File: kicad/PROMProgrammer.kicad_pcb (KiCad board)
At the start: 2 copper layers, 174.5 x 93 mm, 90 parts, among them J1 Control / Program Select Swit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, J2 USB_C_Receptacle_PowerOnly_6P, J3 Conn_01x02, J4 USB_A, J5 Barrel_Jack, Q2 BC108, Q3 BC108, Q4 BD139, Q5 BC108, Q6 BC108, SW1 SW_SPDT, SW11 SW_Push_SPDT, SW12 SW_Push_SPDT, SW13 SW_Push_SPDT, SW14 SW_Push_SPDT, SW15 SW_Push_SPDT, SW16 SW_Push_SPDT, SW17 SW_Push_SPDT, SW18 SW_Push_SPDT, SW2 SW_SPDT, SW3 SW_SPDT, SW4 SW_SPDT, SW5 SW_SPDT, SW6 SW_SPDT, SW8 SW_SPDT, U1 74S188, U2 MC34063AP, U6 4043, U7 4017, U8 HEF4093B, U9 TL431LP

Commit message: Tweak docs
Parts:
- added G003: LOGO, AAA_Project:qr_code, B.Cu at (70.4, 104.6)
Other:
- board text added: "Documentation -->"

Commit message: Starting docs
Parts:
- D10: footprint Diode_THT:D_DO-41_SOD81_P12.70mm_Horizontal -> Diode_THT:D_DO-41_SOD81_P10.16mm_Horizontal
- D14: footprint Diode_THT:D_DO-41_SOD81_P12.70mm_Horizontal -> Diode_THT:D_DO-35_SOD27_P7.62mm_Horizontal
- U1: footprint AAA_Project:DIP-16_W7.62mm_wide_TPH -> Package_DIP:DIP-16_W7.62mm
- U9: footprint Package_TO_SOT_THT:TO-92 -> Package_TO_SOT_THT:TO-92_Inline
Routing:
- net Net-(D14-A): track 33.0 -> 35.1 mm
- net PULSE: track 210.2 -> 211.5 mm
- net Net-(D10-A): track 18.6 -> 19.6 mm

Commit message: Version update
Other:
- board text added: "CS-014"
- board text added: "Version 1.4"
- board text removed: "Version 1.2"
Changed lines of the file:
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@@
 	(title_block
 		(title "PROM Programmer")
-		(date "2025-03-27")
+		(date "2025-04-06")
 		(rev "1.4")
 	)
@@
 		)
 	)
-	(gr_text "Version 1.2"
+	(gr_text "Version 1.4"
 		(at 68.956386 146.978028 0)
 		(layer "F.SilkS")
@@
 		)
 	)
+	(gr_text "CS-014"
+		(at 216.537498 144.623331 0)
+		(layer "B.SilkS")
+		(effects
+			(font
+				(size 1 1)
+				(thickness 0.1)
+			)
+			(justify left bottom mirror)
+		)
+	)

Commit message: Update docs
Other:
- board text added: "OUT IN NC"
- board text added: "Version 1.5"
- board text removed: "Version 1.4"
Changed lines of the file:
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@@
 	(title_block
 		(title "PROM Programmer")
-		(date "2025-04-06")
-		(rev "1.4")
+		(date "2025-04-14")
+		(rev "1.5")
 	)
 	(layers
@@
 		)
 		(property "Value" "10nf"
-			(at 7.907839 2.872547 0)
+			(at 2.254259 -3.410485 0)
 			(layer "F.SilkS")
 			(effects
@@
 		)
 	)
+	(gr_text "OUT IN NC"
+		(at 128.921769 63.828529 0)
+		(layer "F.SilkS")
+		(effects
+			(font
+				(size 1 1)
+				(thickness 0.25)
+				(bold yes)
+			)
+			(justify left bottom)
+		)
+	)
 	(gr_text "1"
 		(at 106.750314 95.513949 0)
@@
 	)
 	(gr_text "On"
-		(at 126.589201 61.29757 0)
+		(at 137.880796 61.224674 0)
 		(layer "F.SilkS")
 		(effects
@@
 		)
 	)
-	(gr_text "Version 1.4"
+	(gr_text "Version 1.5"
 		(at 68.956386 146.978028 0)
 		(layer "F.SilkS")
@@
 	)
 	(gr_text "Off"
-		(at 137.811318 61.407161 0)
+		(at 126.693046 61.44534 0)
 		(layer "F.SilkS")
 		(effects
@@
 	(segment
 		(start 146.466151 105.33421)
-		(end 146.466151 119.091211)
+		(end 146.466151 125.33484)
 		(width 0.5)
 		(layer "F.Cu")
@@
 		(layer "F.Cu")
 		(net 44)
-	)
-	(segment
-		(start 146.466151 119.091211)
-		(end 146.466151 125.33484)
-		(width 0.5)
-		(layer "F.Cu")
-		(net 44)

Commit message: Tidy up & docs
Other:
- board text added: "<-- Program Read -->"
- board text added: "Press To"
- board text added: "Program"
- board text removed: "<-- Program Control -->"
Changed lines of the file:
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@@
 		(layer "Edge.Cuts")
+	)
+	(gr_text "Program"
+		(at 178.790086 85.998869 0)
+		(layer "F.SilkS")
+		(effects
+			(font
+				(size 1.5 1.5)
+				(thickness 0.3)
+				(bold yes)
+			)
+			(justify left bottom)
+		)
 	)
 	(gr_text "1\n\n2\n\n3"
@@
 		)
 	)
-	(gr_text "<-- Program\n\n\n\n    Control -->"
-		(at 208.630704 82.085949 0)
+	(gr_text "<-- Program\n\n\n\n    Read -->"
+		(at 211.071613 82.133825 0)
 		(layer "F.SilkS")
 		(effects
@@
 				(bold yes)
 			)
+			(justify left bottom)
+		)
+	)
+	(gr_text "Press To"
+		(at 178.839736 74.231872 0)
+		(layer "F.SilkS")
+		(effects
+			(font
+				(size 1.5 1.5)
+				(thickness 0.3)
+				(bold yes)
+			)

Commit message: Minor layout changes
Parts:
- added TP7: GND, TestPoint:TestPoint_THTPad_2.0x2.0mm_Drill1.0mm, F.Cu at (117.4, 137.9)
- U1: footprint Package_DIP:DIP-16_W7.62mm -> Socket:DIP_Socket-16_W4.3_W5.08_W7.62_W10.16_W10.9_3M_216-3340-00-0602J
- moved C12 8.92 mm to (138.4, 116.5)
- moved C5 8.53 mm to (110.2, 62.2)
- moved U8 7.80 mm to (128.7, 121.6)
- moved TP1 5.56 mm to (138.2, 108.9)
- moved SW8 5.43 mm to (141.3, 60.7)
- moved TP2 3.28 mm to (113.4, 132.7)
- moved J4 3.20 mm to (159.2, 70.7)
- moved J5 3.20 mm to (173.7, 71.1)
- moved C4 2.47 mm to (142.2, 68.6), turned to -90 degrees
- moved RV1 2.26 mm to (159.2, 102.3)
- moved U7 1.24 mm to (145.2, 114.0)
- moved TP6 1.21 mm to (136.9, 96.1)
- moved R12 0.90 mm to (159.2, 106.2)
- moved TP3 0.73 mm to (109.6, 137.9)
- moved U6 0.72 mm to (161.7, 114.0)
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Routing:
- net +5V: track 308.7 -> 327.0 mm
- net GND: track 762.4 -> 770.6 mm
- net VCC: track 107.5 -> 100.4 mm
- net Net-(J3-Pin_1): track 97.6 -> 91.1 mm
- net Net-(C11-Pad2): track 58.6 -> 64.1 mm
- net Net-(U7-CKEN): track 25.7 -> 30.4 mm
- net Net-(U6-S2): track 47.5 -> 51.9 mm
- net Net-(C12-Pad2): track 27.6 -> 30.5 mm
- net Net-(R12-Pad1): track 5.25 -> 3.91 mm
- net START: track 31.2 -> 29.9 mm
- net Net-(U7-CLK): track 46.2 -> 47.4 mm
- net Net-(U6-S4): track 24.6 -> 23.6 mm
- net Net-(SW6-A): track 58.2 -> 57.4 mm
- net Net-(U6-Q3): track 37.1 -> 36.4 mm
- net Net-(U6-Q2): track 57.3 -> 56.6 mm
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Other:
- board text added: "!!1W HOT!!"
- board text added: "(Optional)"
- board text added: "+5V 0V"
- board text added: "053edf5b-b108-401d-a210-3ba84cfa1f3a"
- board text added: "Default Approx 4.5K"
- board text added: "Push To"
- board text added: "Version 2.0 - Layout Improvements"
- board text removed: "+5V"
- board text removed: "1W HOT!"
- board text removed: "7754d957-f0da-47ec-9f61-362ba0418017"
- board text removed: "Press To"
- board text removed: "Version 1.5"

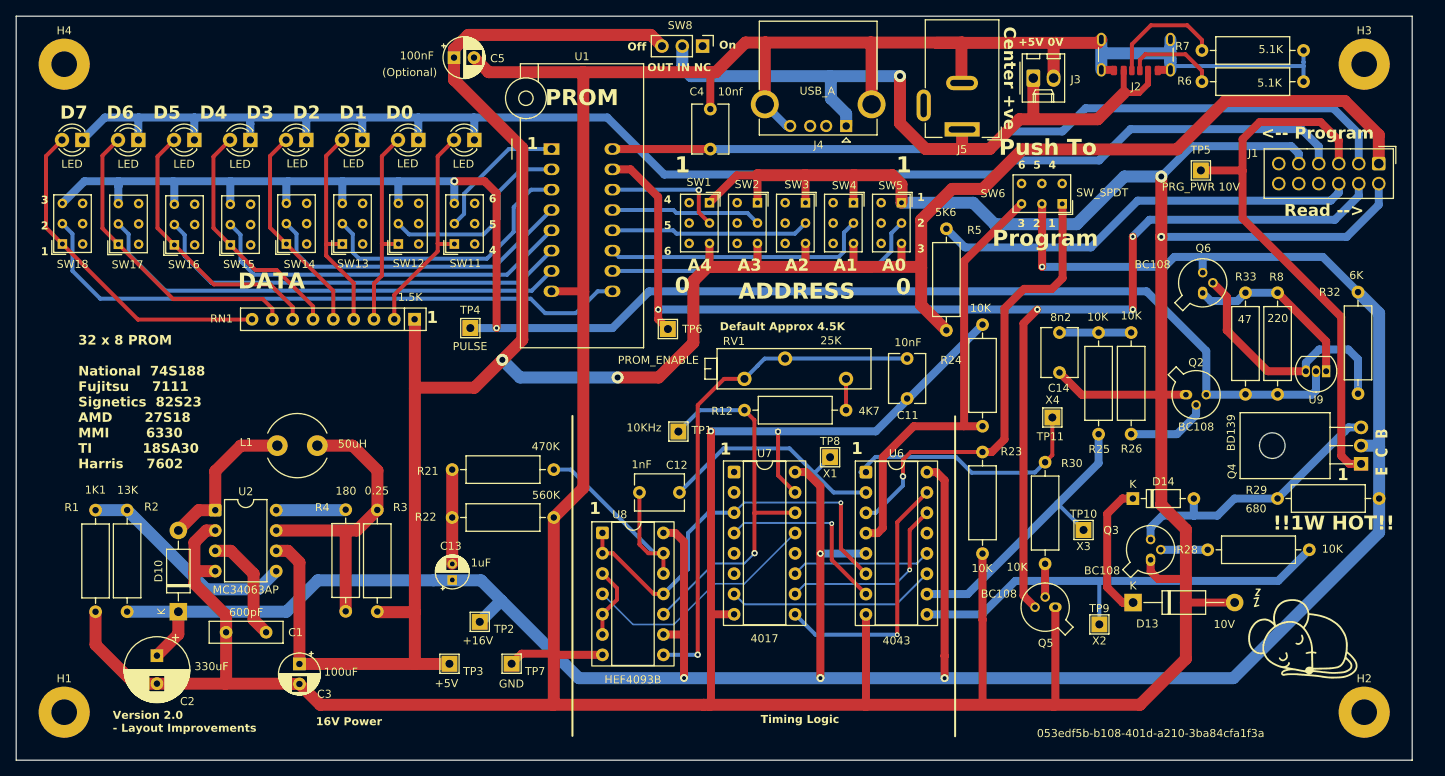
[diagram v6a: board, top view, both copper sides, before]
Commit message: Tweak layout, add part silkscreen values
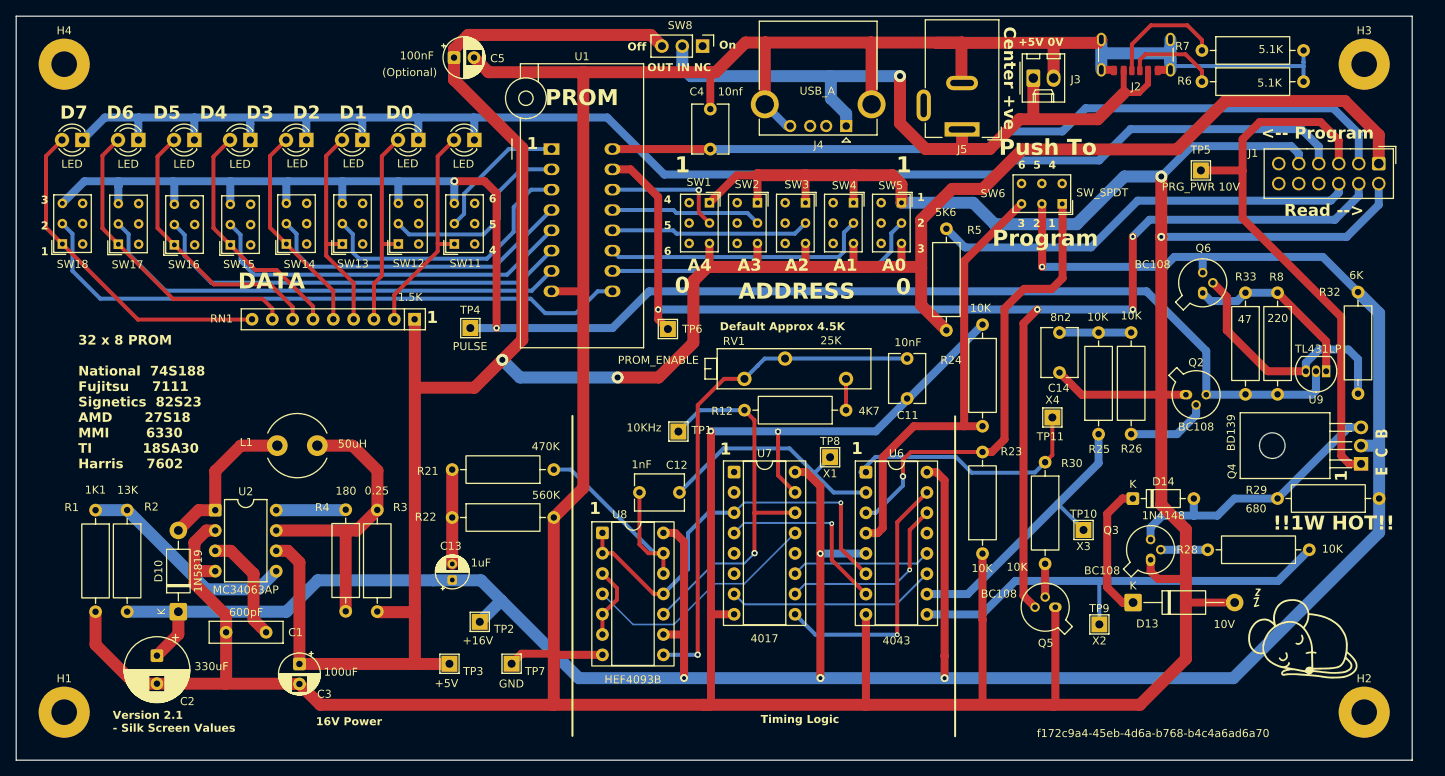
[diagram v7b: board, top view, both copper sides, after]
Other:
- board text added: "Version 2.1 - Silk Screen Values"
- board text added: "f172c9a4-45eb-4d6a-b768-b4c4a6ad6a70"
- board text removed: "053edf5b-b108-401d-a210-3ba84cfa1f3a"
- board text removed: "Version 2.0 - Layout Improvements"

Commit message: Update transistors
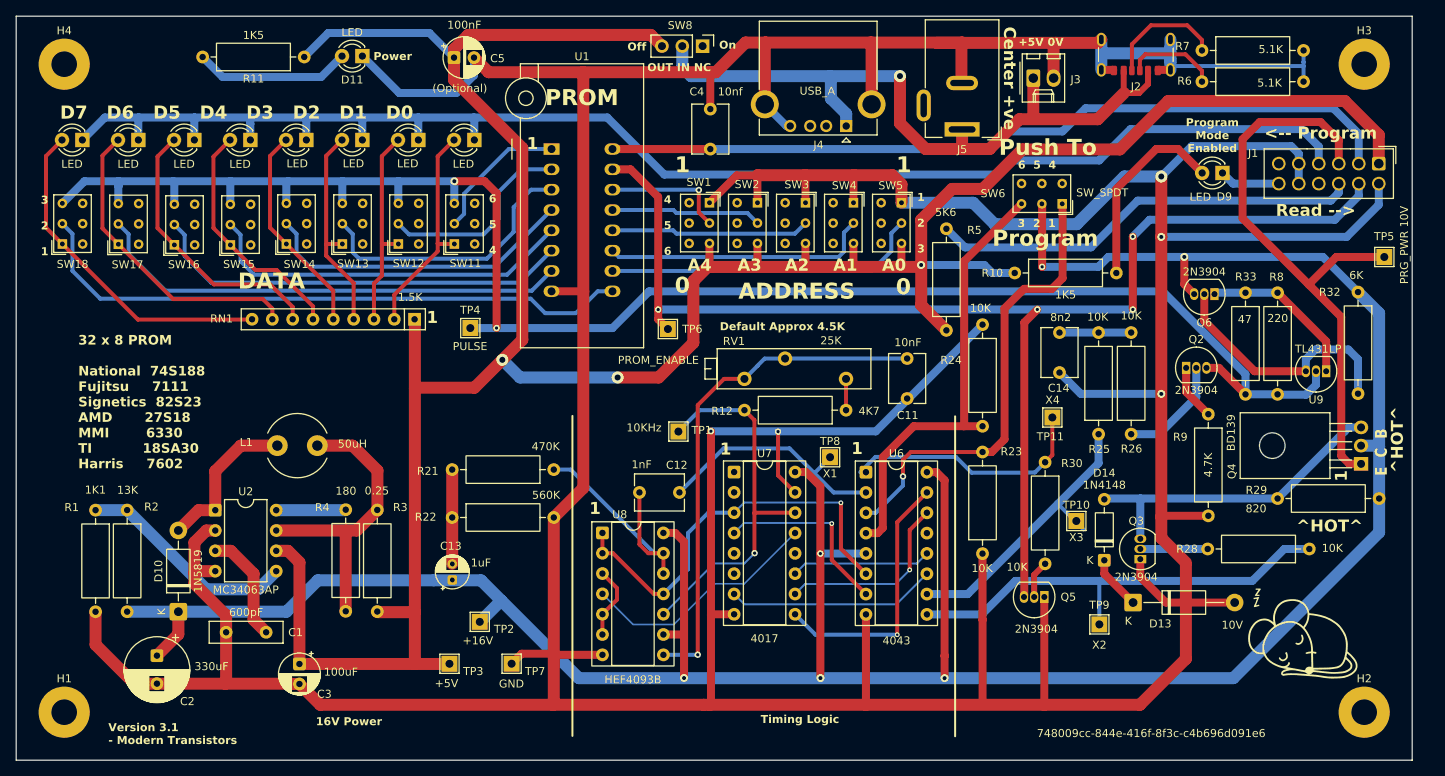
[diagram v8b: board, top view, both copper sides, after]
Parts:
- added D11: LED, LED_THT:LED_D3.0mm, F.Cu at (98.7, 62.0)
- added D9: LED, LED_THT:LED_D3.0mm, F.Cu at (206.2, 76.6)
- added R10: 1K5, Resistor_THT:R_Axial_DIN0309_L9.0mm_D3.2mm_P12.70mm_Horizontal, F.Cu at (180.3, 89.1)
- added R11: 1K5, Resistor_THT:R_Axial_DIN0309_L9.0mm_D3.2mm_P12.70mm_Horizontal, F.Cu at (91.5, 62.1)
- added R9: 4.7K, Resistor_THT:R_Axial_DIN0309_L9.0mm_D3.2mm_P12.70mm_Horizontal, F.Cu at (204.5, 106.7)
- Q2, Q3, Q5, Q6: value BC108 -> 2N3904; footprint Package_TO_SOT_THT:TO-18-3 -> Package_TO_SOT_THT:TO-92_Inline
- R29: value 680 -> 820
- moved TP5 25.4 mm to (226.5, 87.1)
- moved D14 8.50 mm to (191.5, 125.0), turned to 90 degrees
- moved Q2 3.36 mm to (201.7, 100.9)
- moved Q5 1.88 mm to (184.0, 129.6)
- moved Q6 1.48 mm to (205.2, 91.7), turned to 180 degrees
- moved TP10 1.44 mm to (188.0, 120.1)
- moved Q3 1.29 mm to (196.0, 124.9)
- moved R28 0.10 mm to (217.1, 123.6)
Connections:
- J1 pad 11: unconnected-(J1-Pin_11-Pad11) -> GND
- J1 pad 12: unconnected-(J1-Pin_12-Pad12) -> Net-(D9-K)
- Q2 pad 1: GND -> Net-(Q2-E)
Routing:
- net +5V: track 327.0 -> 360.4 mm, vias 2 -> 3
- net GND: track 770.6 -> 798.8 mm, vias 4 -> 5
- net Net-(D9-A): track 0.00 -> 24.5 mm
- net Net-(D11-A): track 0.00 -> 19.5 mm
- net Net-(D13-K): track 17.2 -> 6.06 mm
- net Net-(D9-K): track 0.00 -> 7.59 mm
- net Net-(Q2-E): track 0.00 -> 6.94 mm
- net Net-(D14-A): track 35.1 -> 40.9 mm
- net PRG_PWR: track 69.6 -> 75.2 mm
- net PULSE: track 211.5 -> 215.6 mm
- net Net-(Q2-B): track 10.4 -> 13.7 mm
- net +16V: track 349.7 -> 352.9 mm, vias 5 -> 6
- net Net-(Q3-B): track 5.85 -> 8.42 mm
- net Net-(Q6-E): track 22.5 -> 20.2 mm
- net PROM_ENABLE: track 163.0 -> 160.8 mm
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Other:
- board text added: "748009cc-844e-416f-8f3c-c4b696d091e6"
- board text added: "Power"
- board text added: "Program Mode Enabled"
- board text added: "Version 3.1 - Modern Transistors"
- board text added: "^HOT^"
- board text added: "buymeacoffee is a website that connects developers, designers, artists etc with their communities so that people can express appreciation for their work. If you would like to contribute, feel free to do it at Buy me a coffee!"
- board text added: "https://www.buymeacoffee.com/codesqueak and many thanks in advance."
- board text removed: "!!1W HOT!!"
- board text removed: "Version 2.1 - Silk Screen Values"
- board text removed: "buymeacoffee is a website that connects developers, designers, artists etc with their communities so that people can express appreciation for their work. If you would like to contribute, feel free to do it at Buy me a coffee!, (https://www.buymeacoffee.com/codesqueak), and many thanks in advance."
- board text removed: "f172c9a4-45eb-4d6a-b768-b4c4a6ad6a70"
